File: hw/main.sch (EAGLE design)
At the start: 22 parts, among them IC1 LD33V, IC2 74LS595N, IC3 74LS595N, T1 2N3904, T2 2N3904, T3 2N3904, T4 2N3904, U1 TINY85-20-DIP, U2 TMP36

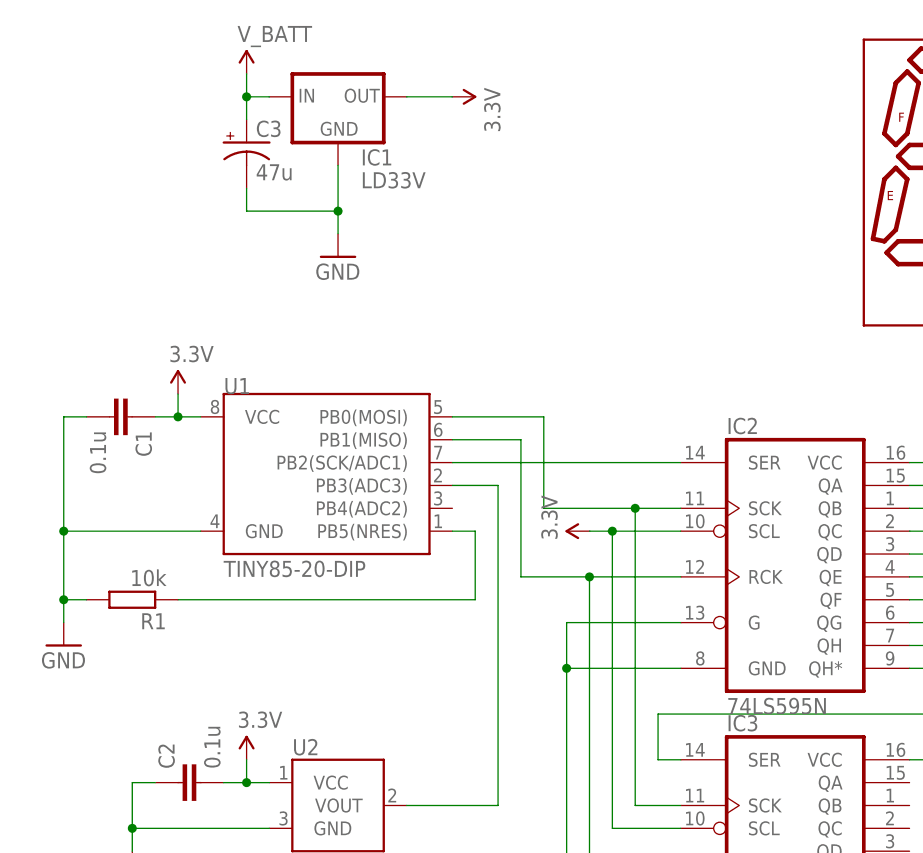
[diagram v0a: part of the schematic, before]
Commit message: Added ICSP header
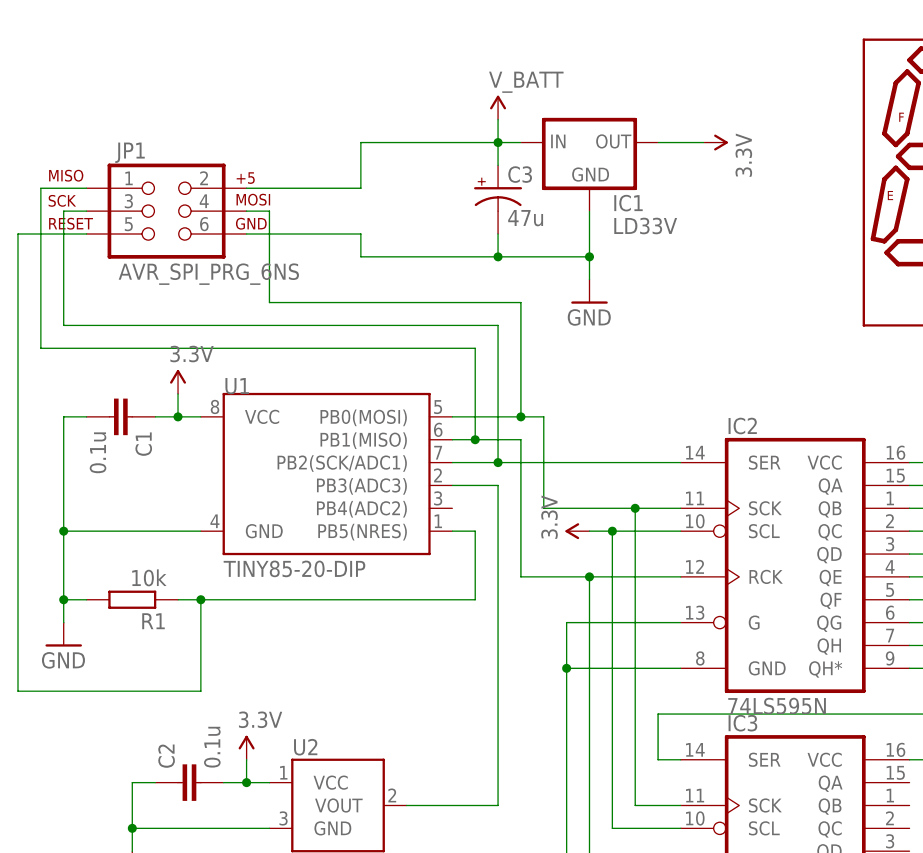
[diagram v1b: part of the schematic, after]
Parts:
- added JP1: AVR_SPI_PRG_6NS, SparkFun-Connectors:AVR_SPI_PRG_6NS
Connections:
- net GND: now also JP1.6
- net N$11: now also JP1.4
- net N$13: now also JP1.1
- net N$31: now also JP1.5
- net N$32: now also JP1.3
- net V_BATT: now also JP1.2
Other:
- moved on the sheet: C3, IC1
